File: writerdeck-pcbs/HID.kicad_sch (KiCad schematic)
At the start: 1 part, among them U1 RP2040

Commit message: power management done
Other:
- note added: "media + keyboard + trackball"
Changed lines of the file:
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@@
 	(generator_version "9.0")
 	(paper "A4")
+	(text "media + keyboard + trackball"
+		(exclude_from_sim no)
+		(at 137.414 62.992 0)
+		(effects
+			(font
+				(size 1.27 1.27)
+			)
+		)
+	)
 	(symbol
 		(lib_id "MCU_RaspberryPi:RP2040")

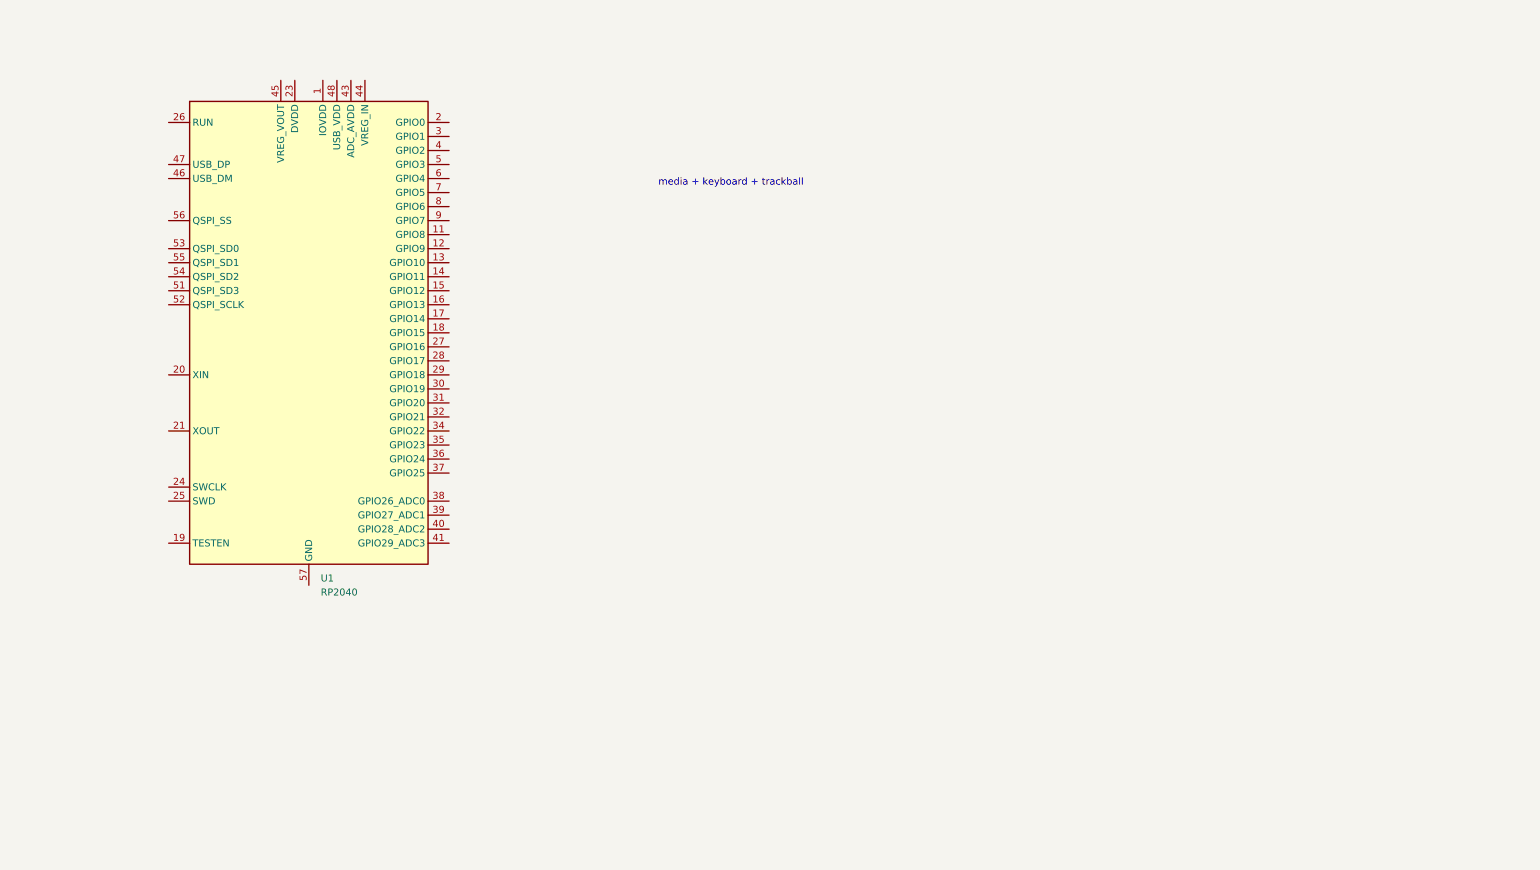
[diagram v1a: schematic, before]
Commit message: pre switch matrix, restructure
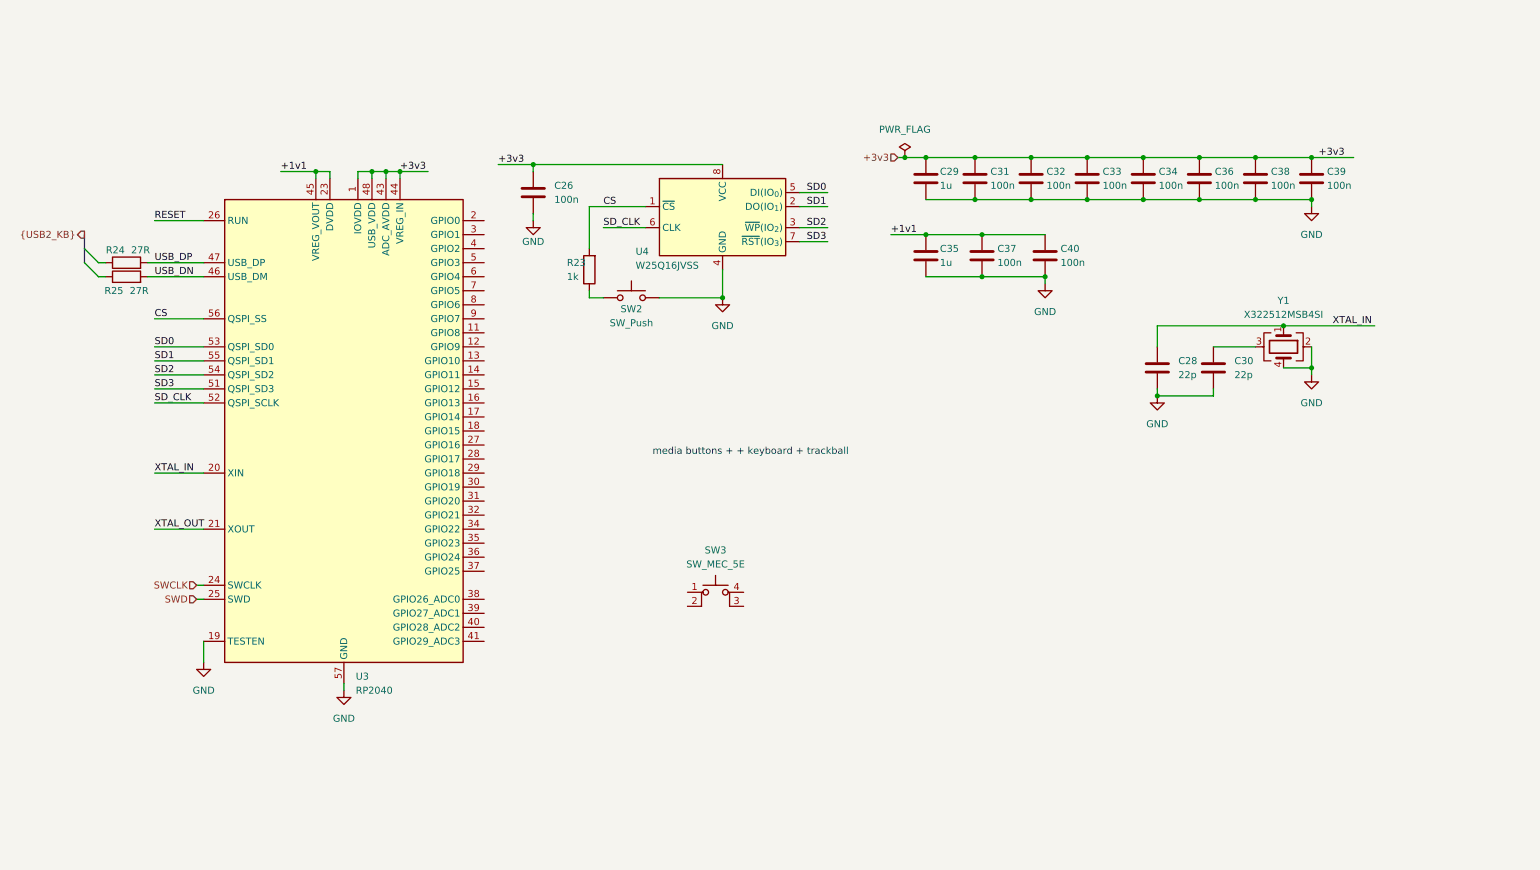
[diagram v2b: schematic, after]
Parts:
- added C26, C31, C32, C33, C34, C36, C37, C38, C39, C40: 100n, Capacitor_SMD:C_0603_1608Metric, symbol ZF_common:100n 5% 0603 Capacitor
- added C28, C30: 22p, Capacitor_SMD:C_0603_1608Metric, symbol ZF_common:22p 5% 0603 Capacitor
- added C29, C35: 1u, Capacitor_SMD:C_0603_1608Metric, symbol ZF_common:1u 10% 0603 Capacitor
- added R23: 1k, Resistor_SMD:R_0603_1608Metric, symbol ZF_common:1k 1% 0603 Resistor
- added R24, R25: 27R, Resistor_SMD:R_0603_1608Metric, symbol ZF_common:27R 1% 0603 Resistor
- added SW2: SW_Push, symbol Switch:SW_Push
- added SW3: SW_MEC_5E, symbol Switch:SW_MEC_5E
- added U4: W25Q16JVSS, Package_SO:SOIC-8_5.3x5.3mm_P1.27mm, symbol ZF_common:W25Q16JVSS
- added Y1: X322512MSB4SI, Crystal:Crystal_SMD_3225-4Pin_3.2x2.5mm, symbol ZF_common:X322512MSB4SI
- renumbered U1 to U3
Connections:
- net +3v3: now reaches U3.1 (IOVDD), U3.10 (IOVDD), U3.22 (IOVDD), U3.33 (IOVDD), U3.42 (IOVDD), U3.49 (IOVDD)
- net +3v3: now also U3.43 (ADC_AVDD), U3.44 (VREG_IN), U3.48 (USB_VDD), C26.1, C29.1, C31.1, C32.1, C33.1, C34.1, C36.1, C38.1, C39.1, U4.8 (VCC)
- net GND: now reaches U3.19 (TESTEN)
- net GND: now also U3.57 (GND), C26.2, C28.2, C29.2, C30.2, C31.2, C32.2, C33.2, C34.2, C35.2, C36.2, C37.2, C38.2, C39.2, C40.2, SW2.2, U4.4 (GND), Y1.2, Y1.4
- net XTAL_IN: now reaches U3.20 (XIN)
- net XTAL_IN: now also C28.1, Y1.1
- net XTAL_OUT: now reaches U3.21 (XOUT)
- net +1v1: now reaches U3.23 (DVDD), U3.50 (DVDD)
- net +1v1: now also U3.45 (VREG_VOUT), C35.1, C37.1, C40.1
- net SWCLK: now reaches U3.24 (SWCLK)
- net SWD: now reaches U3.25 (SWD)
- net RESET: now reaches U3.26 (RUN)
- net USB_DN: now reaches U3.46 (USB_DM)
- net USB_DN: now also R25.2
- net USB_DP: now reaches U3.47 (USB_DP)
- net USB_DP: now also R24.2
- net SD3: now reaches U3.51 (QSPI_SD3)
- net SD3: now also U4.7 (~{RST}(IO_{3}))
- net SD_CLK: now reaches U3.52 (QSPI_SCLK)
- net SD_CLK: now also U4.6 (CLK)
- net SD0: now reaches U3.53 (QSPI_SD0)
- net SD0: now also U4.5 (DI(IO_{0}))
- net SD2: now reaches U3.54 (QSPI_SD2)
- net SD2: now also U4.3 (~{WP}(IO_{2}))
- net SD1: now reaches U3.55 (QSPI_SD1)
- net SD1: now also U4.2 (DO(IO_{1}))
- net CS: now reaches U3.56 (QSPI_SS)
- net CS: now also R23.2, U4.1 (~{CS})
- new net: R23.1, SW2.1
- new net: C30.1, Y1.3
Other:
- note added: "media buttons + + keyboard + trackball"
- note removed: "media + keyboard + trackball"
- moved on the sheet: U3

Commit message: backup
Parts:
- removed SW2: SW_Push, symbol Switch:SW_Push
- removed SW3: SW_MEC_5E, symbol Switch:SW_MEC_5E
- added D10, D11, D12, D13, D14, D15, D16, D17, D19, D20, D21, D22, D23, D24, D25, D26, D27, D28, D29, D30, D31, D32, D33, D34, D35, D36, D37, D38, D39, D4, D40, D41, D42, D43, D44, D45, D46, D47, D48, D49, D5, D6, D8, D9: 1N4148W-TP, Diode_SMD:D_SOD-123, symbol ZF_common:1N4148W-TP
- added SW14, SW15, SW16, SW17, SW18, SW19, SW20, SW21, SW22, SW23, SW25, SW26, SW27, SW28, SW29, SW3, SW30, SW31, SW32, SW33, SW34, SW35, SW36, SW37, SW38, SW39, SW4, SW40, SW41, SW42, SW43, SW44, SW45, SW46, SW47, SW48, SW49, SW5, SW50, SW51, SW52, SW53, SW54, SW55, SW7: Tact Switch, symbol ZF_common:Tact Switch
- added SW2: SKRHABE010, ZF_common:SKRHABE010, symbol ZF_common:SKRHABE010
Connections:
- net GND: now also SW2.5, SW3.4 (A)
- net at R23.1: now also SW3.1, SW3.2
- net COL9: now reaches U3.11 (GPIO8)
- net COL9: now also SW28.1, SW28.2, SW38.1, SW38.2, SW48.1, SW48.2
- net COL10: now reaches U3.12 (GPIO9)
- net COL10: now also SW29.1, SW29.2, SW39.1, SW39.2, SW49.1, SW49.2
- net ROW1: now reaches U3.13 (GPIO10)
- net ROW1: now also D13.1 (K), D14.1 (K), D15.1 (K), D16.1 (K), D17.1 (K), D4.1 (K), D5.1 (K), D6.1 (K)
- net ROW2: now reaches U3.14 (GPIO11)
- net ROW2: now also D10.1 (K), D11.1 (K), D12.1 (K), D19.1 (K), D20.1 (K), D21.1 (K), D22.1 (K), D23.1 (K), D8.1 (K), D9.1 (K)
- net ROW3: now reaches U3.15 (GPIO12)
- net ROW3: now also D24.1 (K), D25.1 (K), D26.1 (K), D27.1 (K), D28.1 (K), D29.1 (K), D30.1 (K), D31.1 (K), D32.1 (K), D33.1 (K)
- net ROW4: now reaches U3.16 (GPIO13)
- net ROW4: now also D34.1 (K), D35.1 (K), D36.1 (K), D37.1 (K), D38.1 (K), D39.1 (K), D40.1 (K), D41.1 (K), D42.1 (K), D43.1 (K)
- net ROW5: now reaches U3.17 (GPIO14)
- net ROW5: now also D44.1 (K), D45.1 (K), D46.1 (K), D47.1 (K), D48.1 (K), D49.1 (K)
- net LMB: now reaches U3.18 (GPIO15)
- net LMB: now also SW2.2
- net COL1: now reaches U3.2 (GPIO0)
- net COL1: now also SW30.1, SW30.2, SW4.1, SW4.2, SW40.1, SW40.2, SW50.1, SW50.2, SW7.1, SW7.2
- net COL2: now reaches U3.3 (GPIO1)
- net COL2: now also SW15.1, SW15.2, SW31.1, SW31.2, SW41.1, SW41.2, SW5.1, SW5.2, SW51.1, SW51.2
- net MOUSE_A: now reaches U3.38 (GPIO26_ADC0)
- net MOUSE_A: now also SW2.1
- net MOUSE_B: now reaches U3.39 (GPIO27_ADC1)
- net MOUSE_B: now also SW2.4
- net COL3: now reaches U3.4 (GPIO2)
- net COL3: now also SW14.1, SW14.2, SW16.1, SW16.2, SW32.1, SW32.2, SW42.1, SW42.2, SW52.1, SW52.2
- net MOUSE_C: now reaches U3.40 (GPIO28_ADC2)
- net MOUSE_C: now also SW2.3
- net MOUSE_D: now reaches U3.41 (GPIO29_ADC3)
- net MOUSE_D: now also SW2.6
- net COL4: now reaches U3.5 (GPIO3)
- net COL4: now also SW17.1, SW17.2, SW19.1, SW19.2, SW33.1, SW33.2, SW43.1, SW43.2, SW53.1, SW53.2
- net COL5: now reaches U3.6 (GPIO4)
- net COL5: now also SW18.1, SW18.2, SW20.1, SW20.2, SW34.1, SW34.2, SW44.1, SW44.2, SW54.1, SW54.2
- net COL6: now reaches U3.7 (GPIO5)
- net COL6: now also SW21.1, SW21.2, SW25.1, SW25.2, SW35.1, SW35.2, SW45.1, SW45.2, SW55.1, SW55.2
- net COL7: now reaches U3.8 (GPIO6)
- net COL7: now also SW22.1, SW22.2, SW26.1, SW26.2, SW36.1, SW36.2, SW46.1, SW46.2
- net COL8: now reaches U3.9 (GPIO7)
- net COL8: now also SW23.1, SW23.2, SW27.1, SW27.2, SW37.1, SW37.2, SW47.1, SW47.2
- new net: D9.2 (A), SW15.3 (K), SW15.4 (A)
- new net: D39.2 (A), SW45.3 (K), SW45.4 (A)
- new net: D41.2 (A), SW47.3 (K), SW47.4 (A)
- new net: D10.2 (A), SW16.3 (K), SW16.4 (A)
- new net: D16.2 (A), SW22.3 (K), SW22.4 (A)
- new net: D24.2 (A), SW30.3 (K), SW30.4 (A)
- new net: D17.2 (A), SW23.3 (K), SW23.4 (A)
- new net: D13.2 (A), SW19.3 (K), SW19.4 (A)
- new net: D32.2 (A), SW38.3 (K), SW38.4 (A)
- new net: D43.2 (A), SW49.3 (K), SW49.4 (A)
- new net: D44.2 (A), SW50.3 (K), SW50.4 (A)
- new net: D46.2 (A), SW52.3 (K), SW52.4 (A)
- new net: D31.2 (A), SW37.3 (K), SW37.4 (A)
- new net: D6.2 (A), SW5.3 (K), SW5.4 (A)
- new net: D4.2 (A), SW14.3 (K), SW14.4 (A)
- new net: D45.2 (A), SW51.3 (K), SW51.4 (A)
- new net: D47.2 (A), SW53.3 (K), SW53.4 (A)
- new net: D23.2 (A), SW29.3 (K), SW29.4 (A)
- new net: D20.2 (A), SW26.3 (K), SW26.4 (A)
- new net: D34.2 (A), SW40.3 (K), SW40.4 (A)
- new net: D36.2 (A), SW42.3 (K), SW42.4 (A)
- new net: D14.2 (A), SW20.3 (K), SW20.4 (A)
- new net: D11.2 (A), SW17.3 (K), SW17.4 (A)
- new net: D37.2 (A), SW43.3 (K), SW43.4 (A)
- new net: D48.2 (A), SW54.3 (K), SW54.4 (A)
- new net: D25.2 (A), SW31.3 (K), SW31.4 (A)
- new net: D22.2 (A), SW28.3 (K), SW28.4 (A)
- new net: D28.2 (A), SW34.3 (K), SW34.4 (A)
- new net: D21.2 (A), SW27.3 (K), SW27.4 (A)
- new net: D26.2 (A), SW32.3 (K), SW32.4 (A)
- new net: D5.2 (A), SW4.3 (K), SW4.4 (A)
- new net: D15.2 (A), SW21.3 (K), SW21.4 (A)
- new net: D35.2 (A), SW41.3 (K), SW41.4 (A)
- new net: D49.2 (A), SW55.3 (K), SW55.4 (A)
- new net: D8.2 (A), SW7.3 (K), SW7.4 (A)
- new net: D30.2 (A), SW36.3 (K), SW36.4 (A)
- new net: D19.2 (A), SW25.3 (K), SW25.4 (A)
- new net: D40.2 (A), SW46.3 (K), SW46.4 (A)
- new net: D38.2 (A), SW44.3 (K), SW44.4 (A)
- new net: D33.2 (A), SW39.3 (K), SW39.4 (A)
- new net: D27.2 (A), SW33.3 (K), SW33.4 (A)
- new net: D29.2 (A), SW35.3 (K), SW35.4 (A)
- new net: D12.2 (A), SW18.3 (K), SW18.4 (A)
- new net: D42.2 (A), SW48.3 (K), SW48.4 (A)
- no-connect marks 0 -> 10
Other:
- note removed: "media buttons + + keyboard + trackball"
- moved on the sheet: C26, C28, C29, C30, C31, C32, C33, C34, C35, C36, C37, C38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
